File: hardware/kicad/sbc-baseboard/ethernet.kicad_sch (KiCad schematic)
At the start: 25 parts, among them J10 RJ45 magjack 10/100, U301 KSZ8081RNA, Y301 25MHz

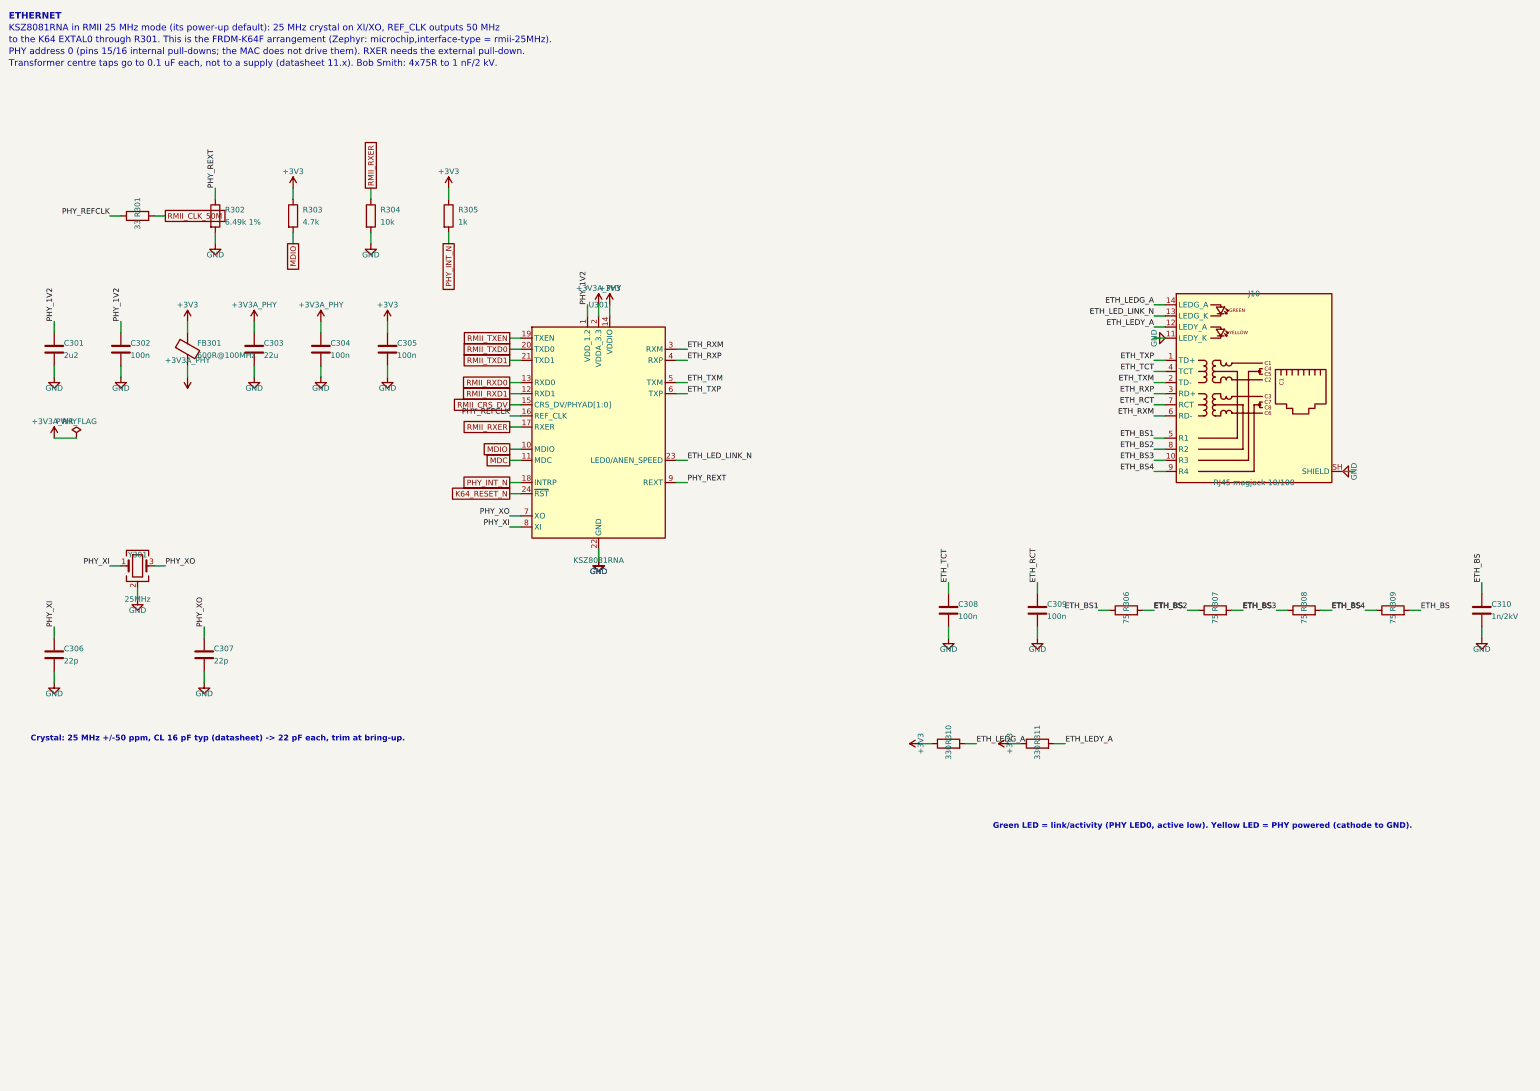
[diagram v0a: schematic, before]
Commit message: Re-lay out every sheet around its main component
Nets fan out of each hub IC as wires at pin pitch; connectors, series
parts, pull-ups and power symbols sit at the lane ends, and labels are
kept for nets that leave the page. Supply pins share a bus with their
decoupling; ESD arrays sit on the connector's D-/D+ rows and port
switches on the VBUS row, so every wire into a receptacle is straight;
the stacked USB-A is a two-unit symbol, one per port. Relays move to
their own sheet (8xx). ESD diodes use KiCad's PESD5V0S1UL in SOD-882.

Generator: gen/fanout.py (lane engine), gen/check_geom.py (endpoint
contacts), gen/netcheck.py (wire-level rail merges). ERC, both checks
and a renumbering-tolerant netlist diff against the first pass all
clean; 331 parts, 354 nets.

Co-Authored-By: Claude Fable 5.1 <noreply@anthropic.com>
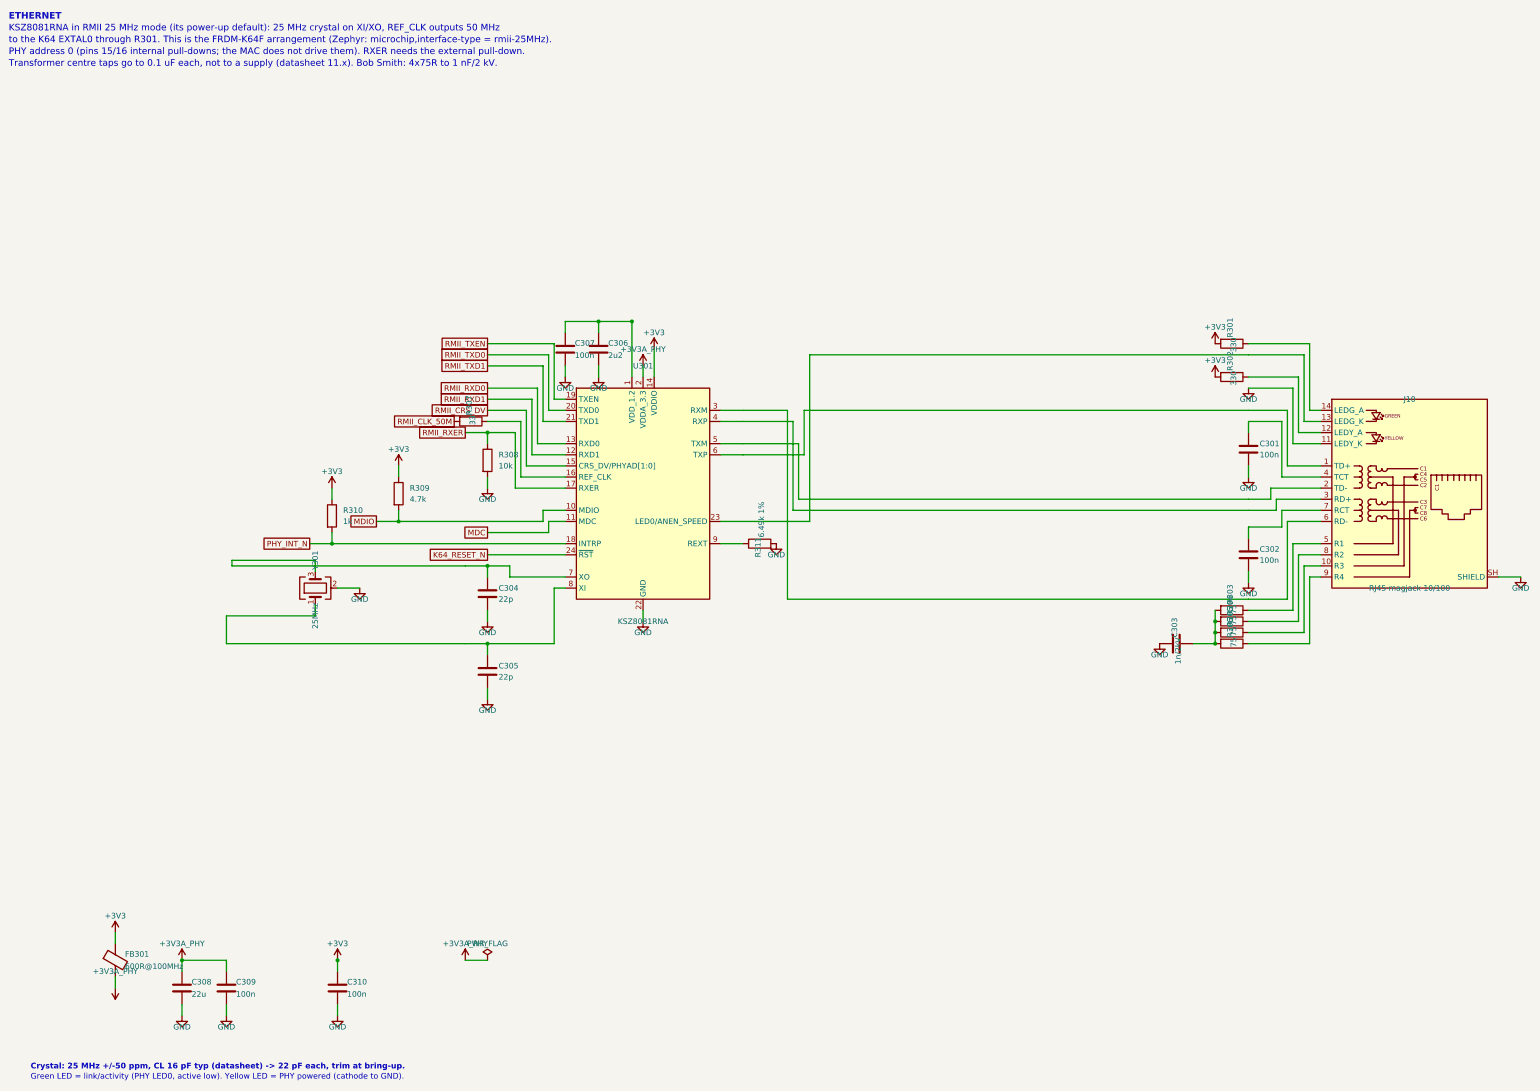
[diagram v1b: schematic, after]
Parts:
- C301: value 2u2 -> 100n
- C303: value 22u -> 1n/2kV; footprint Capacitor_SMD:C_0805_2012Metric -> Capacitor_SMD:C_1206_3216Metric
- C304, C305: value 100n -> 22p
- C306: value 22p -> 2u2
- C307: value 22p -> 100n
- C308: value 100n -> 22u; footprint Capacitor_SMD:C_0603_1608Metric -> Capacitor_SMD:C_0805_2012Metric
- C310: value 1n/2kV -> 100n; footprint Capacitor_SMD:C_1206_3216Metric -> Capacitor_SMD:C_0603_1608Metric
- R301: value 33 -> 330
- R302: value 6.49k 1% -> 330
- R303: value 4.7k -> 75
- R304: value 10k -> 75
- R305: value 1k -> 75
- R307: value 75 -> 33
- R308: value 75 -> 10k
- R309: value 75 -> 4.7k
- R310: value 330 -> 1k
- R311: value 330 -> 6.49k 1%
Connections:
- net +3V3: now also C310.1, R301.2, R302.2, R309.1; no longer C305.1, R303.1, R305.1, R311.1
- net +3V3A_PHY: now also C308.1, C309.1; no longer C303.1, C304.1
- net GND: now also R308.2, R311.2; no longer R302.2, R304.2
- net MDIO: now also R309.2; no longer R303.2
- net PHY_INT_N: now also R310.2; no longer R305.2
- net RMII_CLK_50M: now also R307.2; no longer R301.2
- net RMII_RXER: now also R308.1; no longer R304.1
- removed net ETH_BS: C310.1, R306.2, R307.2, R308.2, R309.2
- net ETH_BS1: no longer names the net of J10.5 (R1)
- net ETH_BS1: now also R303.1; no longer R306.1
- net ETH_BS2: no longer names the net of J10.8 (R2)
- net ETH_BS2: now also R304.1; no longer R307.1
- net ETH_BS3: no longer names the net of J10.10 (R3)
- net ETH_BS3: now also R305.1; no longer R308.1
- net ETH_BS4: no longer names the net of J10.9 (R4)
- net ETH_BS4: now also R306.1; no longer R309.1
- net ETH_LEDG_A: no longer names the net of J10.14 (LEDG_A)
- net ETH_LEDG_A: now also R301.1; no longer R310.2
- net ETH_LEDY_A: no longer names the net of J10.12 (LEDY_A)
- net ETH_LEDY_A: now also R302.1; no longer R311.2
- net ETH_LED_LINK_N: no longer names the net of J10.13 (LEDG_K), U301.23 (LED0/ANEN_SPEED)
- net ETH_RCT: no longer names the net of J10.7 (RCT)
- net ETH_RCT: now also C302.1; no longer C309.1
- net ETH_RXM: no longer names the net of J10.6 (RD-), U301.3 (RXM)
- net ETH_RXP: no longer names the net of J10.3 (RD+), U301.4 (RXP)
- net ETH_TCT: no longer names the net of J10.4 (TCT)
- net ETH_TCT: now also C301.1; no longer C308.1
- net ETH_TXM: no longer names the net of J10.2 (TD-), U301.5 (TXM)
- net ETH_TXP: no longer names the net of J10.1 (TD+), U301.6 (TXP)
- removed net PHY_1V2: C301.1, C302.1, U301.1 (VDD_1.2)
- net PHY_REFCLK: no longer names the net of U301.16 (REF_CLK)
- net PHY_REFCLK: now also R307.1; no longer R301.1
- net PHY_REXT: no longer names the net of U301.9 (REXT)
- net PHY_REXT: now also R311.1; no longer R302.1
- net PHY_XI: no longer names the net of U301.8 (XI), Y301.1
- net PHY_XI: now also C305.1; no longer C306.1
- net PHY_XO: no longer names the net of U301.7 (XO), Y301.3
- net PHY_XO: now also C304.1; no longer C307.1
- new net: C306.1, C307.1, U301.1 (VDD_1.2)
- new net: C303.1, R303.2, R304.2, R305.2, R306.2

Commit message: Symbol direction, field text and decoupling ladders across every sheet
Every GND symbol now hangs down and every rail stands up: decoupling
hangs from the supply bus into a GND rail with one GND symbol at the end
(ladders), rails on crowded supply pins are jogged sideways, the SWD
header is mirrored instead of rotated. Field text on in-line parts reads
horizontally (KiCad adds the symbol rotation to the field angle) and is
placed by lane direction; hanging parts carry their text on the side away
from the pin; IC reference and value sit where the library put them.
Power sheet: bus buffer moved under the STUSB4500's I2C lanes with direct
routes, programmer by label, buck drawn as a box with its input and
output capacitors as ladders. New gen/check_layout.py reports text and
wire overlaps and wrong-way power symbols; PDF export draws hop-overs.

ERC 0, no merged rails, netlist equivalent; text-overlap residue listed
in the layout checker output remains on the hub, relays and DAPLink.

Co-Authored-By: Claude Fable 5.1 <noreply@anthropic.com>
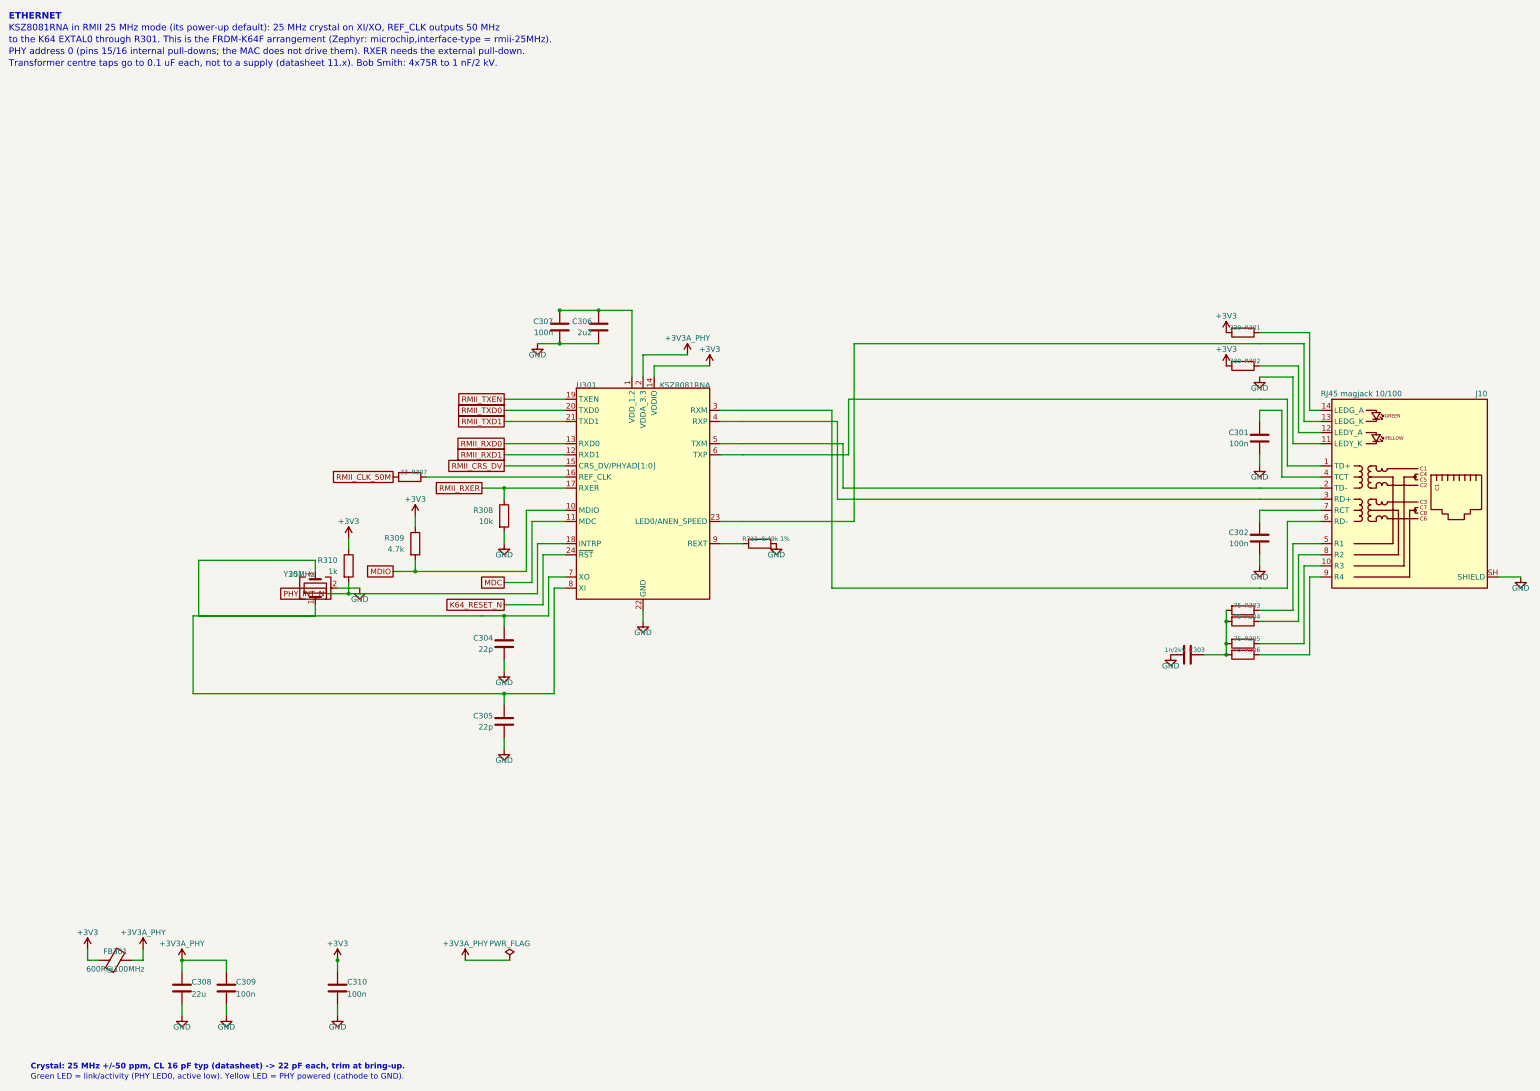
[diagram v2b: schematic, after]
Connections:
- net at C304.1, U301.7 (XO), Y301.3: now also C305.1, U301.8 (XI), Y301.1

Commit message: Placement pass: every sheet clean on all four layout gates
Hanging parts now sit with their near pin between rows, so a pull-up on
the next lane crosses only its lead; parts slide past a neighbour's parts
and text, not its plain wire, and never let a wire run through a body or
a rail symbol. Chains on top/bottom pins run sideways first. Route
channels are numbered per route. Power symbols that would land on a
neighbouring wire get a jog or a hook. The VBUS sense divider moved to
the K64's ADC pin so J3's VBUS lane is a short stretch the ESD array taps;
the J1 tap sits before its divider. Relay coil clusters are drawn by the
engine. Port switches moved so OUT stays on the VBUS row.

ERC 0, no endpoint contacts, no merged rails, no wires through bodies,
no inverted power symbols, on all eight sheets; netlist equivalent to the
first pass (331 parts, 354 nets); USB D+/D-, VBUS and I2C paths verified
pin by pin.

Co-Authored-By: Claude Fable 5.1 <noreply@anthropic.com>
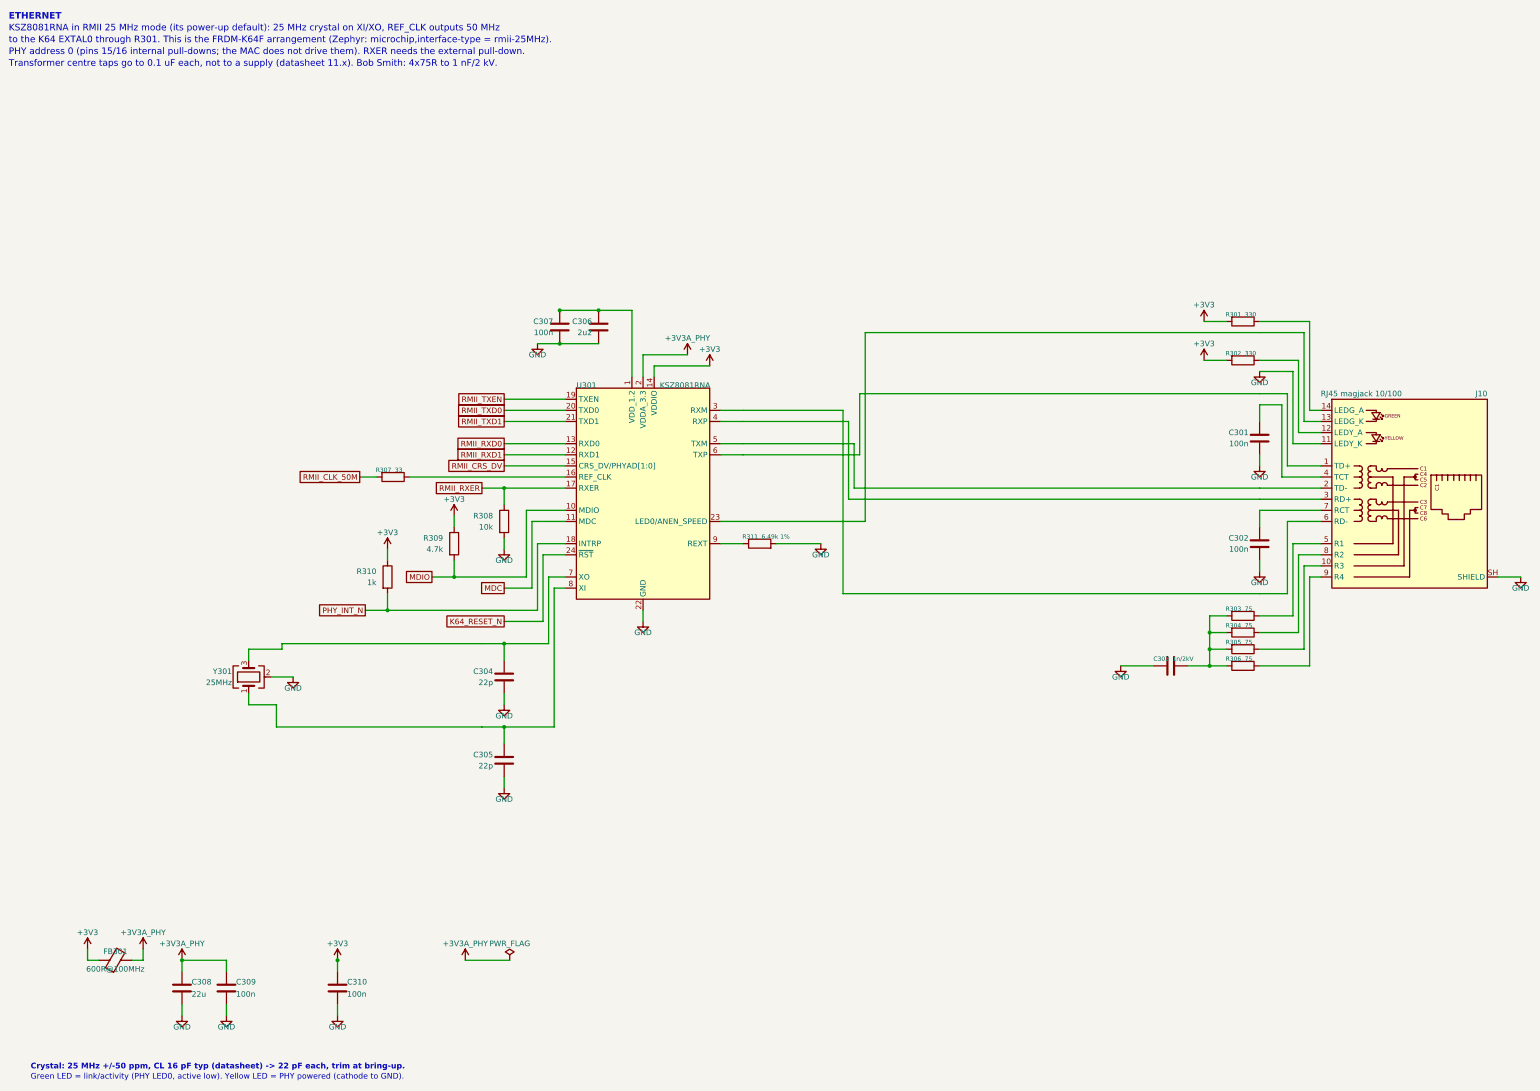
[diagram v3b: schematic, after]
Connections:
- net at C304.1, U301.7 (XO), Y301.3: no longer C305.1, U301.8 (XI), Y301.1
- new net: C305.1, U301.8 (XI), Y301.1
